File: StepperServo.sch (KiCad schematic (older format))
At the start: 14 parts

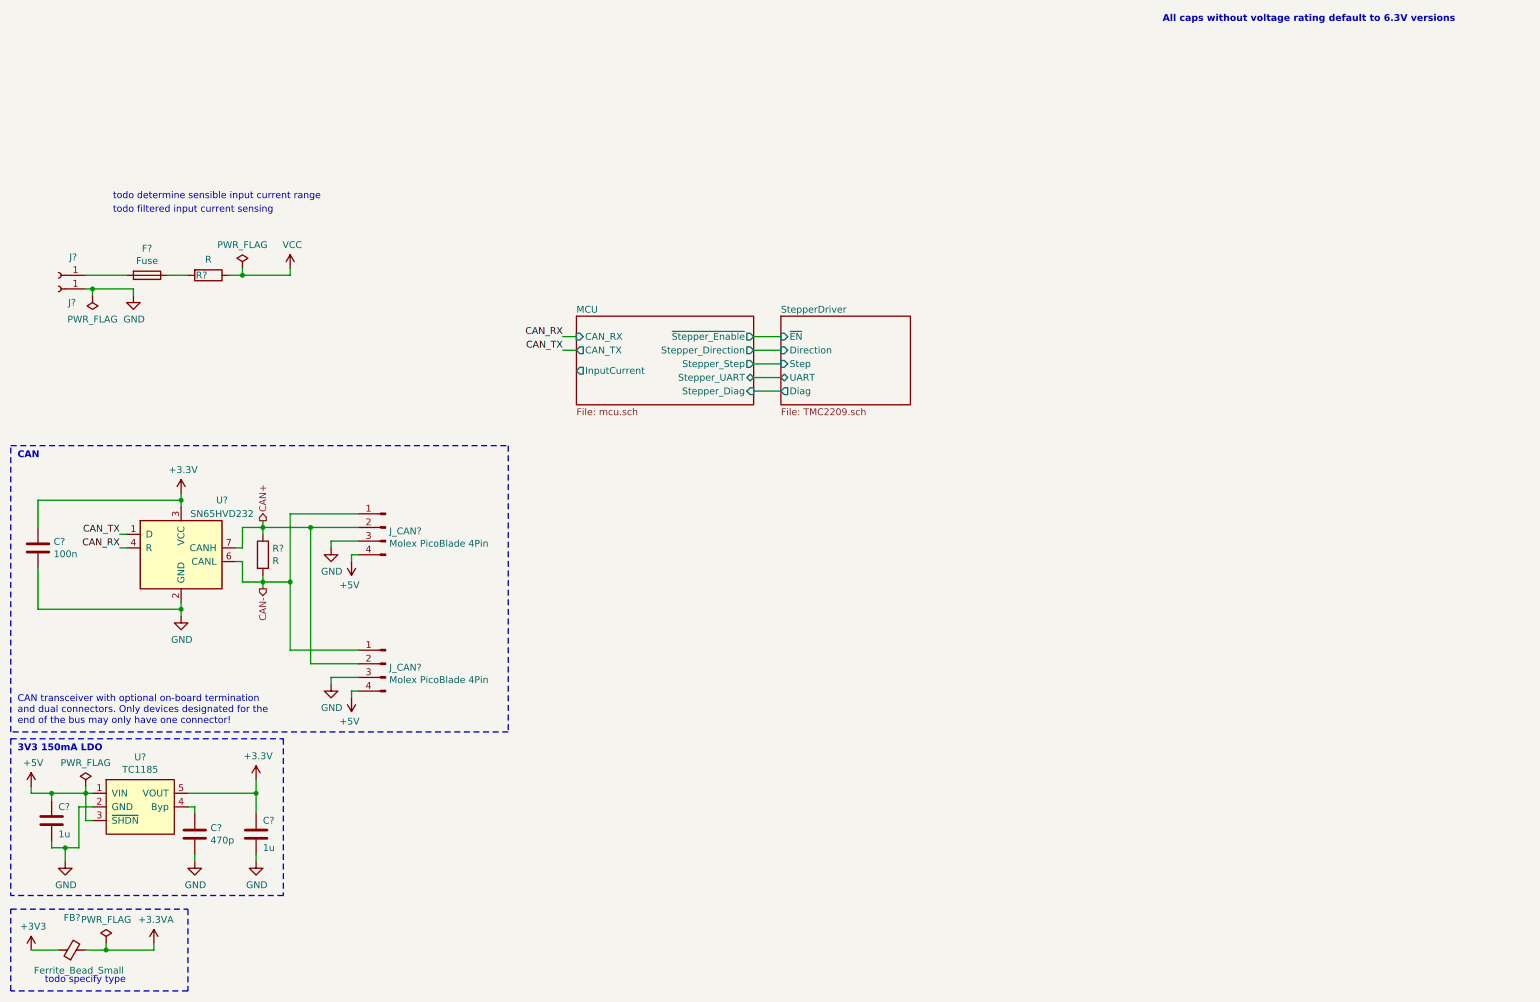
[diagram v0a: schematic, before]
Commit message: Specified dual led resistors Consolidated all grounds to just gnd Consolidated all 3.3 rails to just 3.3V Removed right endstop Removed right wheel angle, servo angle calibration button
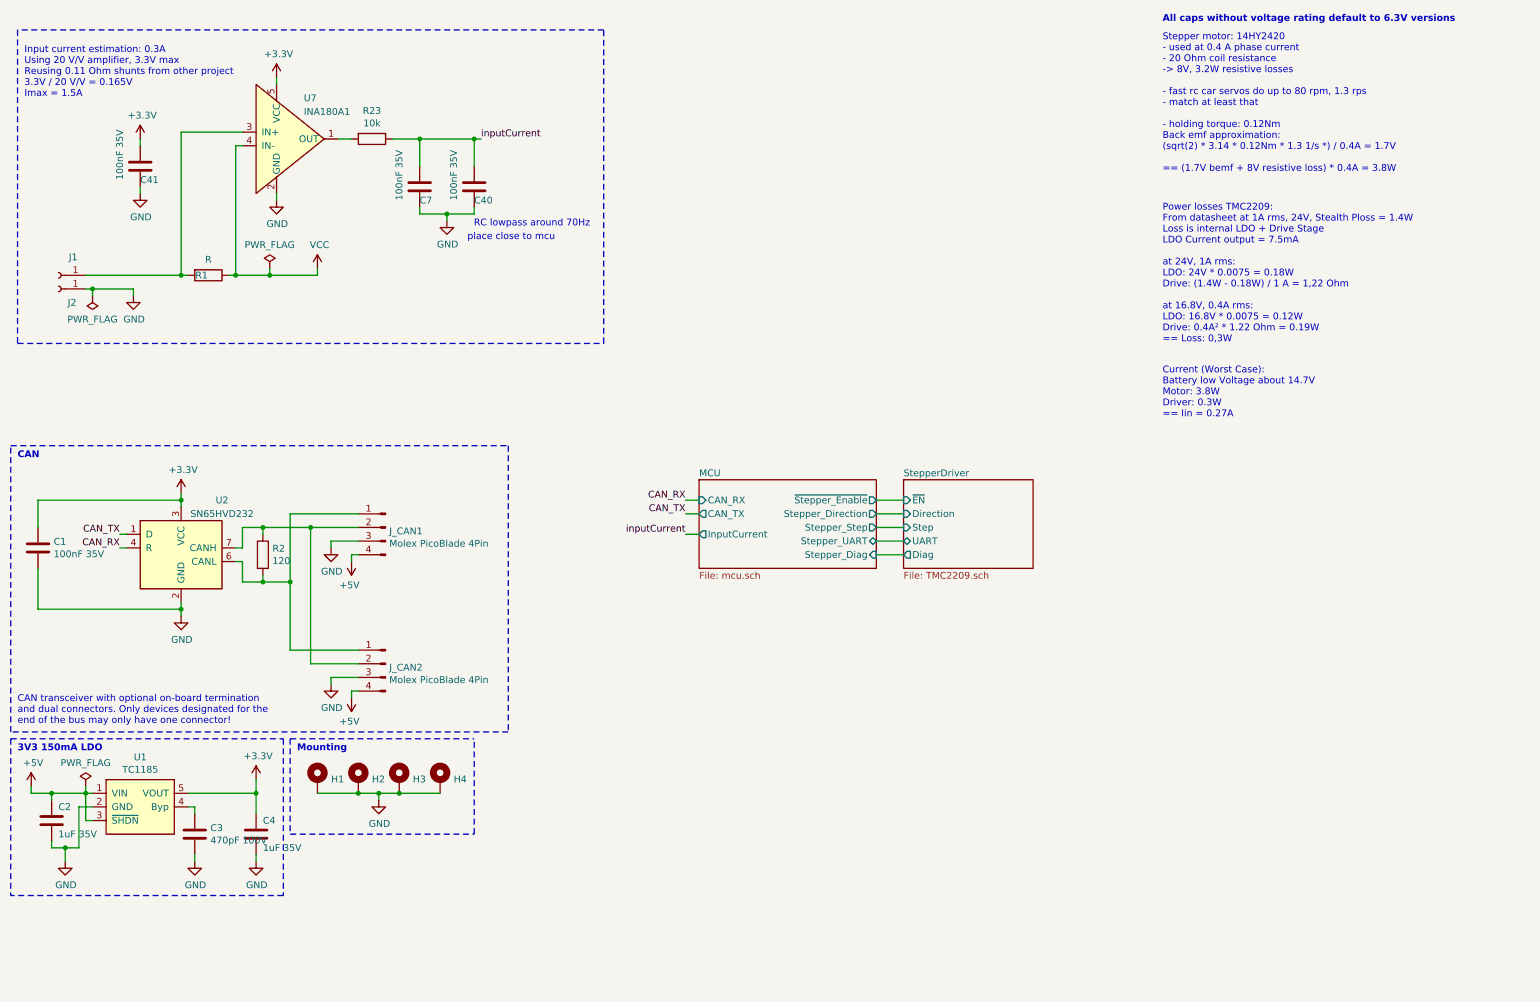
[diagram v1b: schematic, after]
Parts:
- removed F?: Fuse, symbol Device:Fuse
- removed FB?: Ferrite_Bead_Small, symbol Device:Ferrite_Bead_Small
- added C40, C41, C7: 100nF 35V, Capacitor_SMD:C_0603_1608Metric, symbol Device:C
- added H1, H2, H3, H4: MountingHole_Pad, MountingHole:MountingHole_3.2mm_M3_Pad_Via, symbol Mechanical:MountingHole_Pad
- added R23: 10k, Resistor_SMD:R_0603_1608Metric, symbol Device:R
- added U7: INA180A1, Package_TO_SOT_SMD:SOT-23-5, symbol ti:INA180A1
- C1: renamed from C?; value 100n -> 100nF 35V
- C2, C4: renamed from C?; value 1u -> 1uF 35V
- C3: renamed from C?; value 470p -> 470pF 100V
- R1: renamed from R?; footprint (none) -> Resistor_SMD:R_0612_1632Metric
- R2: renamed from R?; value R -> 120
- U1: renamed from U?; footprint (none) -> Package_TO_SOT_SMD:SOT-23-5
- gave numbers to parts that had none: 5
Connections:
- net +3V3: now also C41.1, U7.5 (VCC)
- net GND: now also C40.2, C41.2, C7.2, H1.1, H2.1, H3.1, H4.1, U7.2 (GND)
- net VCC: now also U7.4 (IN-)
- net at R1.2: now also J1.1 (Pin_1), U7.3 (IN+)
- net CAN+: no longer names the net of J_CAN1.2 (Pin_2), J_CAN2.2 (Pin_2), R2.1, U2.7 (CANH)
- net CAN-: no longer names the net of J_CAN1.1 (Pin_1), J_CAN2.1 (Pin_1), R2.2, U2.6 (CANL)
- new net: R23.2, U7.1 (OUT)
- new net inputCurrent: C40.1, C7.1, R23.1
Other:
- note added: "Current (Worst Case):\nBattery low Voltage about 14.7V\nMotor: 3.8W\nDriver: 0.3W\n== Iin = 0.27A\n"
- note added: "Input current estimation: 0.3A\nUsing 20 V/V amplifier, 3.3V max\nReusing 0.11 Ohm shunts from other project\n3.3V / 20 V/V = 0.165V \nImax = 1.5A"
- note added: "Mounting"
- note added: "Power losses TMC2209:\nFrom datasheet at 1A rms, 24V, Stealth Ploss = 1.4W\nLoss is internal LDO + Drive Stage\nLDO Current output = 7.5mA\n\nat 24V, 1A rms: \nLDO: 24V * 0.0075 = 0.18W\nDrive: (1.4W - 0.18W) / 1 A = 1,22 Ohm\n\nat 16.8V, 0.4A rms: \nLDO: 16.8V * 0.0075 = 0.12W\nDrive: 0.4A² * 1.22 Ohm = 0.19W\n== Loss: 0,3W"
- note added: "RC lowpass around 70Hz"
- note added: "Stepper motor: 14HY2420\n- used at 0.4 A phase current \n- 20 Ohm coil resistance\n-> 8V, 3.2W resistive losses\n\n- fast rc car servos do up to 80 rpm, 1.3 rps\n- match at least that\n\n- holding torque: 0.12Nm\nBack emf approximation:\n(sqrt(2) * 3.14 * 0.12Nm * 1.3 1/s *) / 0.4A = 1.7V\n\n== (1.7V bemf + 8V resistive loss) * 0.4A = 3.8W"
- note added: "place close to mcu"
- note removed: "todo determine sensible input current range"
- note removed: "todo filtered input current sensing"
- note removed: "todo specify type"

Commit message: wip layout
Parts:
- R1: value R -> 1.1R
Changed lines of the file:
@@
 P 2000 2450
 F 0 "R1" V 2000 2400 50  0000 C CNN
-F 1 "R" V 1884 2450 50  0000 C CNN
+F 1 "1.1R" V 1884 2450 50  0000 C CNN
 F 2 "Resistor_SMD:R_0612_1632Metric" V 1930 2450 50  0001 C CNN
 F 3 "~" H 2000 2450 50  0001 C CNN

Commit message: Finished v1 layout Added pictures to readme
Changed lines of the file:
@@
 F7 "Stepper_UART" B R 6900 4400 50
 F8 "~Stepper_Enable" O R 6900 4100 50
-F9 "InputCurrent" O L 5600 4350 50
+F9 "InputCurrent" I L 5600 4350 50
 $EndSheet
 Text Notes 9000 600  0    50   ~ 10

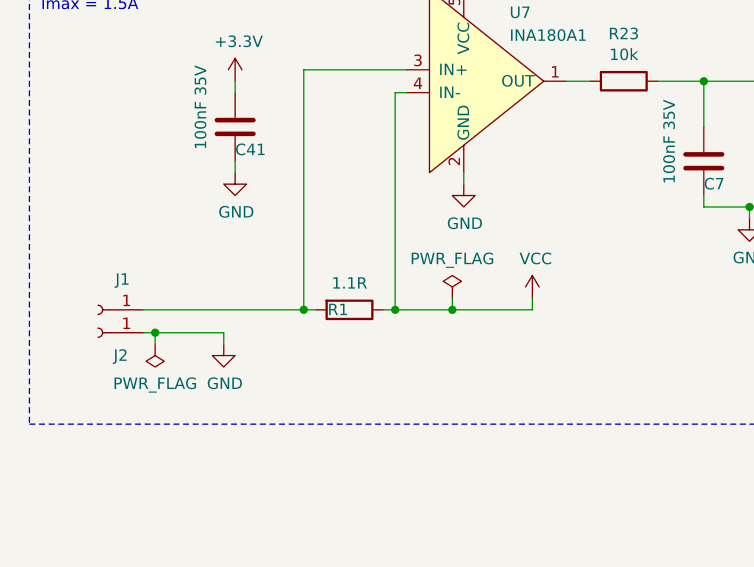
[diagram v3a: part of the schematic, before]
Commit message: fixed wrong shunt ohm value
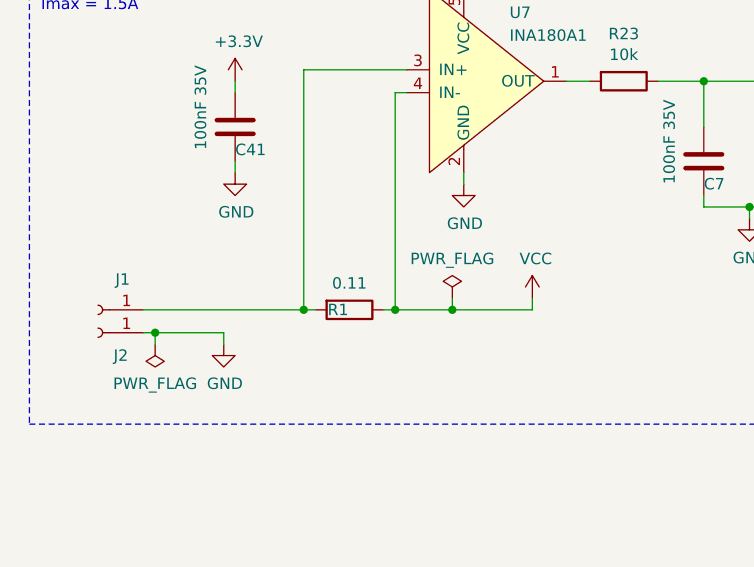
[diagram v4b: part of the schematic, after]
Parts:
- R1: value 1.1R -> 0.11
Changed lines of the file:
@@
 P 2000 2450
 F 0 "R1" V 2000 2400 50  0000 C CNN
-F 1 "1.1R" V 1884 2450 50  0000 C CNN
+F 1 "0.11" V 1884 2450 50  0000 C CNN
 F 2 "Resistor_SMD:R_0612_1632Metric" V 1930 2450 50  0001 C CNN
 F 3 "~" H 2000 2450 50  0001 C CNN
